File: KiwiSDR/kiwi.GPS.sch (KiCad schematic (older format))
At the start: 33 parts, among them J3 SMA, J4 DNL U.FL, U101 SE4150L, U104 LP5907 3.3V 250mA, X101 16.368 MHz

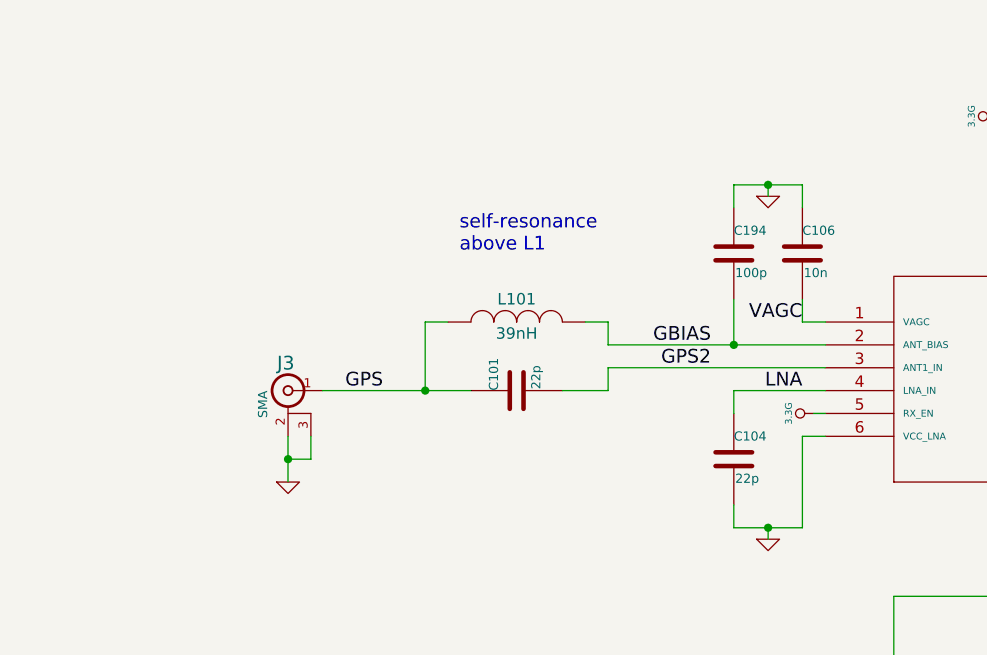
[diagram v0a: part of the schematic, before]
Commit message: long overdue update to v1.0 PCB files
These are the files used in the current production PCBs.
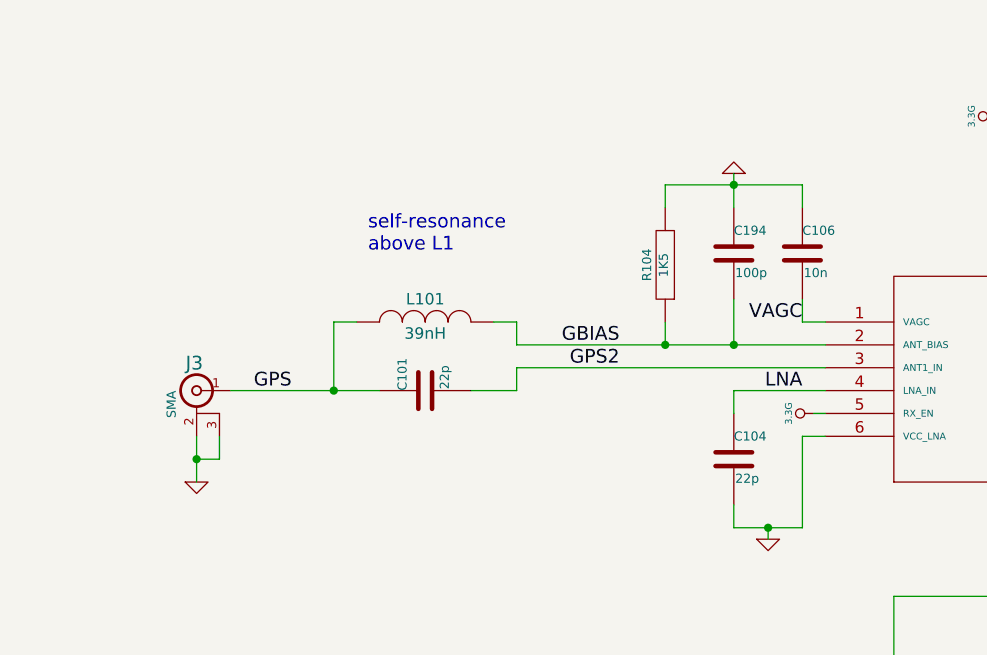
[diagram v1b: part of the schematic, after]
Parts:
- added R104: 1K5, kiwi-SM0402, symbol R
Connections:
- net GBIAS: now also R104.1
- net GND: now also R104.2
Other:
- moved on the sheet: C101, J3, L101
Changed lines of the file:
@@
-EESchema Schematic File Version 2  date Sunday, February 21, 2016 12:56:59 PM
+EESchema Schematic File Version 2  date Monday, May 02, 2016 01:09:56 PM
 LIBS:kiwi
 LIBS:kiwi-cache
@@
 encoding utf-8
 Sheet 3 7
-Title "KiwiSDR Prototype, March 2016"
-Date "20 feb 2016"
-Rev "0.5"
+Title "KiwiSDR, May 2016"
+Date "2 may 2016"
+Rev "1.0"
 Comp "John Seamons, ZL/KF6VO"
 Comment1 ""
@@
 	1    0    0    -1
 $EndComp
-Text Label 5850 3800 2    60   ~ 0
+Text Label 5450 3800 2    60   ~ 0
 GPS2
-Text Label 4250 3900 0    60   ~ 0
+Text Label 3850 3900 0    60   ~ 0
 GPS
 $Comp
 L GND #PWR046
 U 1 1 52B64B99
-P 4000 4300
-F 0 "#PWR046" H 4000 4300 30  0001 C CNN
-F 1 "GND" H 4000 4230 30  0001 C CNN
-F 2 "" H 4000 4300 60  0000 C CNN
-F 3 "" H 4000 4300 60  0000 C CNN
-	1    4000 4300
+P 3600 4300
+F 0 "#PWR046" H 3600 4300 30  0001 C CNN
+F 1 "GND" H 3600 4230 30  0001 C CNN
+F 2 "" H 3600 4300 60  0000 C CNN
+F 3 "" H 3600 4300 60  0000 C CNN
+	1    3600 4300
 	1    0    0    -1
 $EndComp
@@
 L C C101
 U 1 1 52B6718C
-P 5000 3900
-F 0 "C101" H 5000 4000 40  0000 L CNN
-F 1 "22p" H 5006 3815 40  0000 L CNN
-F 2 "kiwi-SM0402" H 5038 3750 30  0001 C CNN
-F 3 "~" H 5000 3900 60  0000 C CNN
-	1    5000 3900
+P 4600 3900
+F 0 "C101" H 4600 4000 40  0000 L CNN
+F 1 "22p" H 4606 3815 40  0000 L CNN
+F 2 "kiwi-SM0402" H 4638 3750 30  0001 C CNN
+F 3 "~" H 4600 3900 60  0000 C CNN
+	1    4600 3900
 	0    -1   -1   0
 $EndComp
@@
 L COIL L101
 U 1 1 52B6711C
-P 5000 3600
-F 0 "L101" H 5000 3700 50  0000 C CNN
-F 1 "39nH" H 5000 3550 50  0000 C CNN
-F 2 "kiwi-SM0402" V 5150 3700 50  0001 C CNN
-F 3 "~" V 5300 3700 60  0001 C CNN
-	1    5000 3600
-	1    0    0    -1
-$EndComp
-Text Label 5850 3700 2    60   ~ 0
+P 4600 3600
+F 0 "L101" H 4600 3700 50  0000 C CNN
+F 1 "39nH" H 4600 3550 50  0000 C CNN
+F 2 "kiwi-SM0402" V 4750 3700 50  0001 C CNN
+F 3 "~" V 4900 3700 60  0001 C CNN
+	1    4600 3600
+	1    0    0    -1
+$EndComp
+Text Label 5450 3700 2    60   ~ 0
 GBIAS
 $Comp
@@
 L GND #PWR048
 U 1 1 52B6876D
-P 6100 3050
-F 0 "#PWR048" H 6100 3050 30  0001 C CNN
-F 1 "GND" H 6100 2980 30  0001 C CNN
-F 2 "" H 6100 3050 60  0000 C CNN
-F 3 "" H 6100 3050 60  0000 C CNN
-	1    6100 3050
-	1    0    0    -1
+P 5950 2950
+F 0 "#PWR048" H 5950 2950 30  0001 C CNN
+F 1 "GND" H 5950 2880 30  0001 C CNN
+F 2 "" H 5950 2950 60  0000 C CNN
+F 3 "" H 5950 2950 60  0000 C CNN
+	1    5950 2950
+	-1   0    0    1
 $EndComp
 $Comp
@@
 	0    -1   -1   0
 $EndComp
-Text Notes 4750 3300 0    60   ~ 0
+Text Notes 4350 3300 0    60   ~ 0
 self-resonance\nabove L1
 $Comp
 L COAX_CONN_3P J3
 U 1 1 52C0A14E
-P 4000 3900
-F 0 "J3" H 4010 4020 60  0000 C CNN
-F 1 "SMA" V 4110 3840 40  0000 C CNN
-F 2 "kiwi-SMA_OPL_EM" H 4000 3900 60  0001 C CNN
-F 3 "~" H 4000 3900 60  0000 C CNN
-	1    4000 3900
+P 3600 3900
+F 0 "J3" H 3610 4020 60  0000 C CNN
+F 1 "SMA" V 3710 3840 40  0000 C CNN
+F 2 "kiwi-SMA_OPL_EM" H 3600 3900 60  0001 C CNN
+F 3 "~" H 3600 3900 60  0000 C CNN
+	1    3600 3900
 	-1   0    0    -1
 $EndComp
@@
 RING
 Wire Wire Line
-	6350 3800 5400 3800
+	5000 3800 6350 3800
 Wire Wire Line
 	7450 2700 7450 3100
@@
 	7650 3100 7650 3000
 Wire Wire Line
-	4150 3900 4800 3900
-Wire Wire Line
-	4000 4100 4000 4300
-Wire Wire Line
-	4600 3600 4600 3900
-Connection ~ 4600 3900
-Wire Wire Line
-	5400 3700 6350 3700
-Wire Wire Line
-	5950 3500 5950 3700
+	3750 3900 4400 3900
+Wire Wire Line
+	3600 4100 3600 4300
+Wire Wire Line
+	4200 3600 4200 3900
+Connection ~ 4200 3900
+Wire Wire Line
+	5000 3700 6350 3700
+Wire Wire Line
+	5950 3700 5950 3500
 Connection ~ 5950 3700
 Wire Wire Line
@@
 	6350 4000 6300 4000
 Wire Wire Line
-	5950 3100 5950 3000
-Wire Wire Line
-	5950 3000 6250 3000
+	5950 2950 5950 3100
+Wire Wire Line
+	5650 3000 6250 3000
 Wire Wire Line
 	6250 3000 6250 3100
-Wire Wire Line
-	6100 3000 6100 3050
-Connection ~ 6100 3000
 Wire Wire Line
 	6350 3900 5950 3900
@@
 Wire Wire Line
 	8150 5750 8100 5750
-Connection ~ 4000 4200
-Wire Wire Line
-	4100 4100 4100 4200
+Connection ~ 3600 4200
+Wire Wire Line
+	3700 4100 3700 4200
 Wire Wire Line
 	10050 4200 10050 4250
@@
 Connection ~ 11450 3900
 Wire Wire Line
-	4100 4200 4000 4200
+	3700 4200 3600 4200
 Wire Wire Line
 	7900 7100 7900 7300
@@
 	8550 3600 8550 3550
 Wire Wire Line
-	4700 3600 4600 3600
-Wire Wire Line
-	5300 3600 5400 3600
-Wire Wire Line
-	5400 3600 5400 3700
-Wire Wire Line
-	5200 3900 5400 3900
-Wire Wire Line
-	5400 3900 5400 3800
+	4300 3600 4200 3600
+Wire Wire Line
+	4900 3600 5000 3600
+Wire Wire Line
+	5000 3600 5000 3700
+Wire Wire Line
+	4800 3900 5000 3900
+Wire Wire Line
+	5000 3900 5000 3800
 Wire Wire Line
 	7150 4600 7150 4800
@@
 Wire Wire Line
 	11450 4200 11450 4250
+$Comp
+L R R104
+U 1 1 5726A558
+P 5650 3350
+F 0 "R104" V 5730 3350 40  0000 C CNN
+F 1 "1K5" V 5657 3351 40  0000 C CNN
+F 2 "kiwi-SM0402" V 5580 3350 30  0001 C CNN
+F 3 "~" H 5650 3350 30  0000 C CNN
+	1    5650 3350
+	-1   0    0    1
+$EndComp
+Wire Wire Line
+	5650 3100 5650 3000
+Connection ~ 5950 3000
+Wire Wire Line
+	5650 3600 5650 3700
+Connection ~ 5650 3700
 $EndSCHEMATC
